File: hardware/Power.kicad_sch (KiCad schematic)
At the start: 39 parts, among them Q1 Q_NMOS, Q2 Q_NMOS, Q3 Q_NMOS, Q4 Q_NMOS, U5 BQ25798RQMR

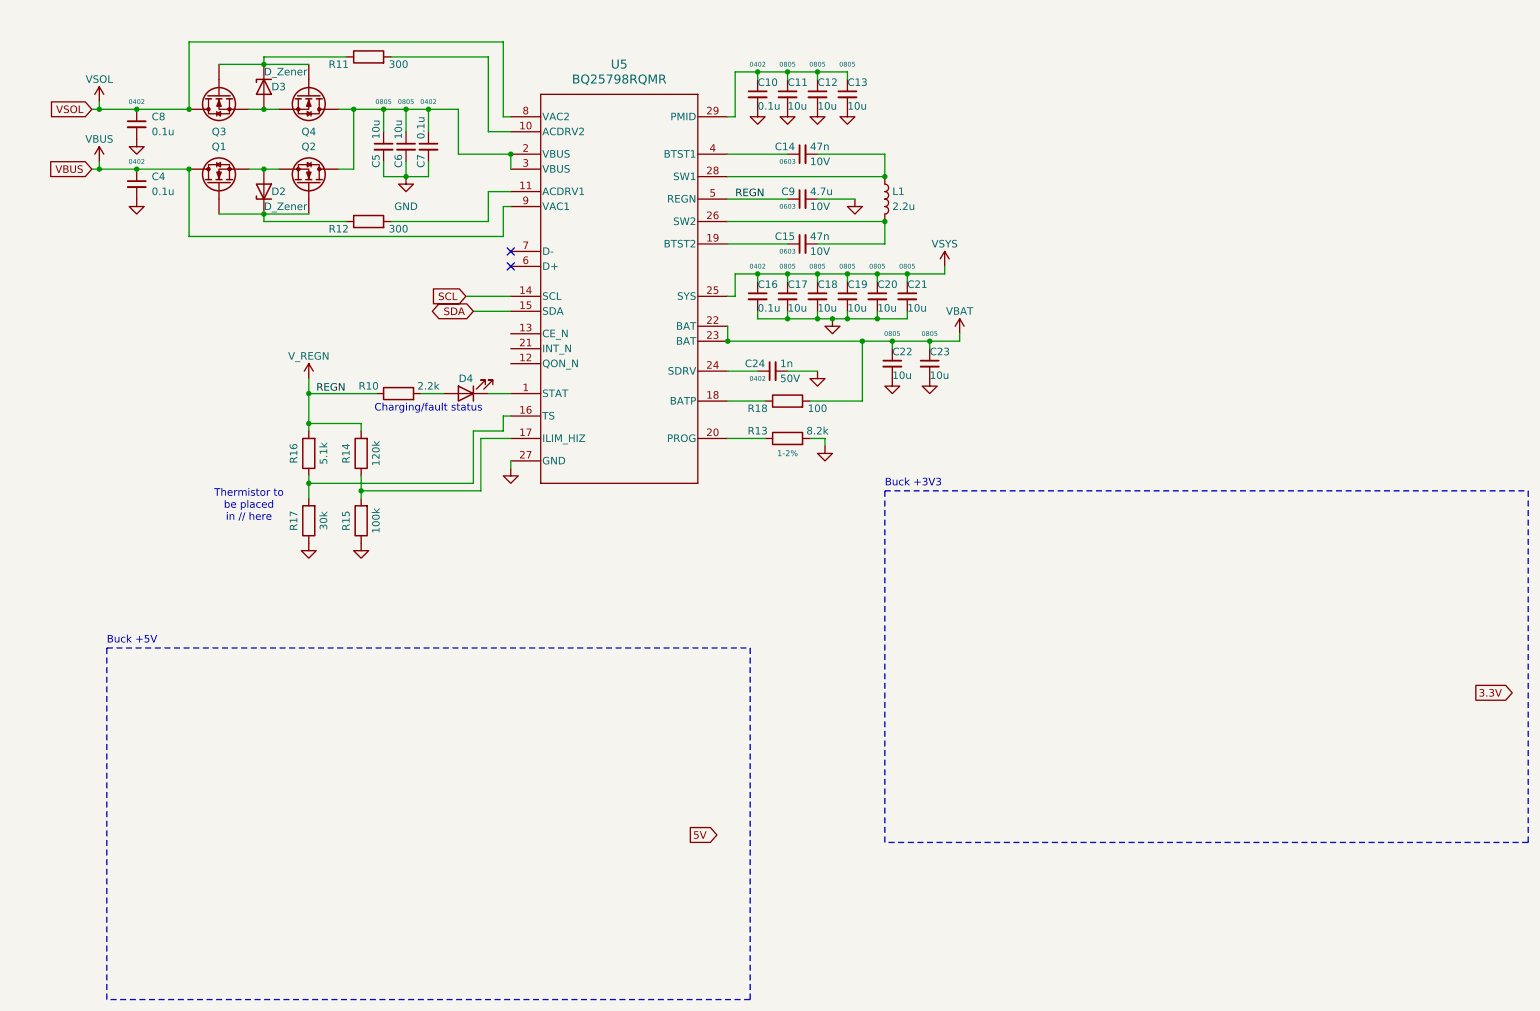
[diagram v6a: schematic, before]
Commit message: Added solar input protection & diodes footprints
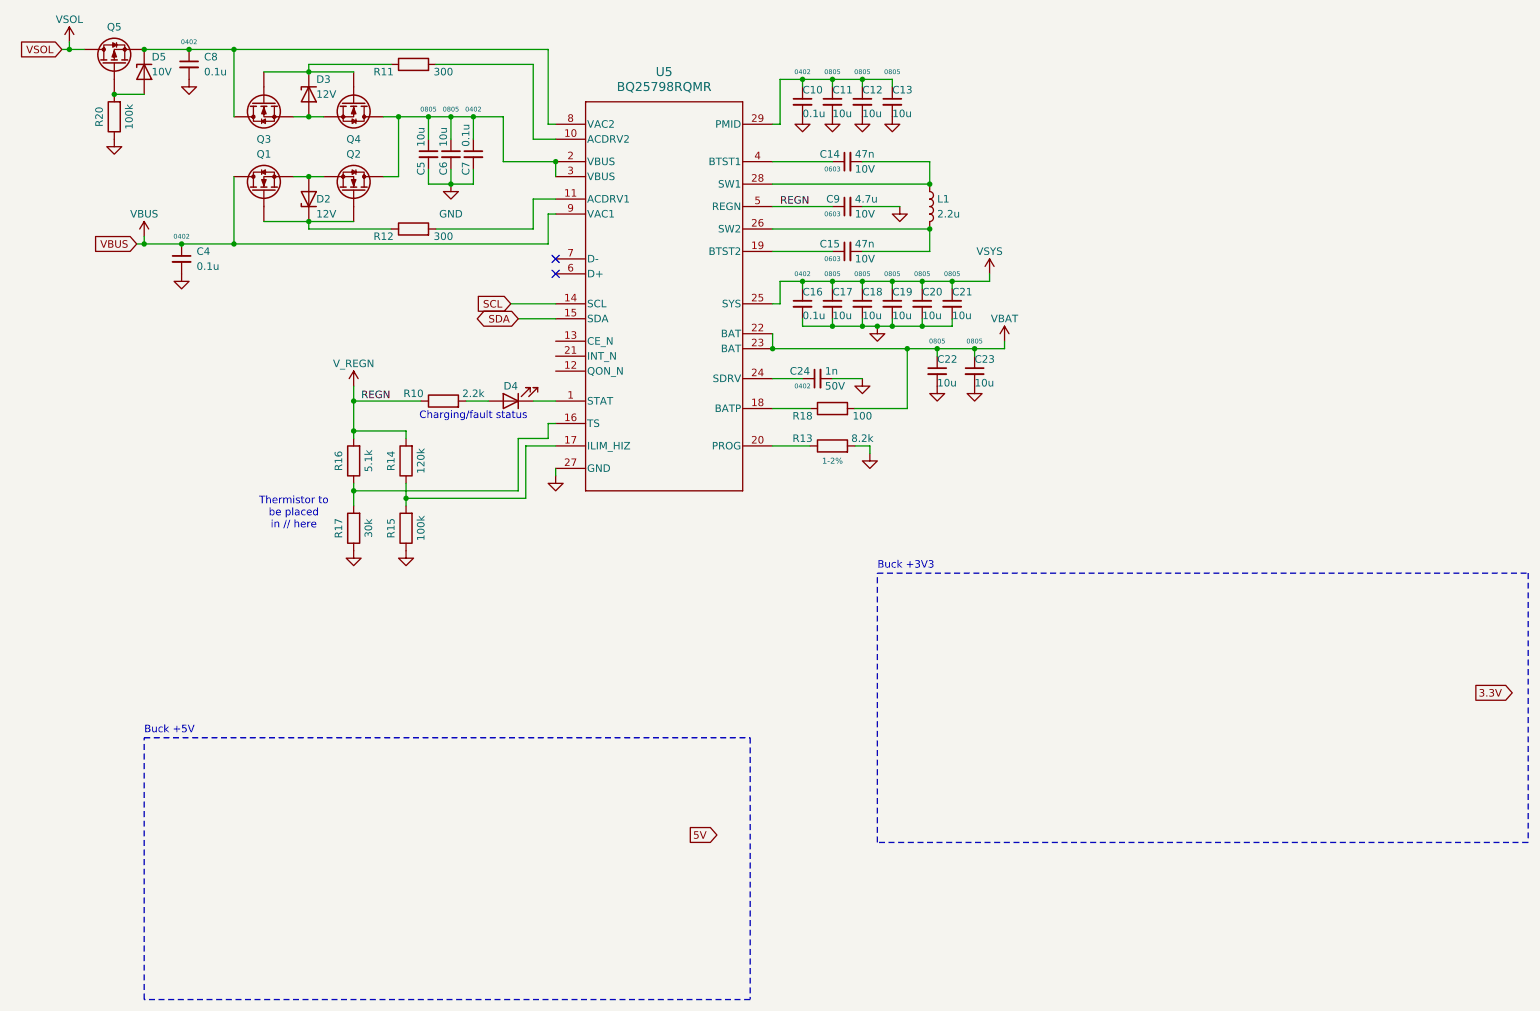
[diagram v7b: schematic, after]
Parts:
- added D5: D_Zener, Diode_SMD:D_SOD-123, symbol Device:D_Zener
- added Q5: Q_PMOS, symbol Device:Q_PMOS
- added R20: 100k, Resistor_SMD:R_0402_1005Metric, symbol Device:R
- D2, D3: footprint (none) -> Diode_SMD:D_SOD-123; Voltage (none) -> 12V
- D4: footprint (none) -> LED_SMD:LED_0603_1608Metric
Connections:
- net GND: now also R20.1
- net VSOL: now also Q5.D; no longer C8.1, Q3.D, U5.8 (VAC2)
- new net: D5.2 (A), Q5.G, R20.2
- new net: C8.1, D5.1 (K), Q3.D, Q5.S, U5.8 (VAC2)
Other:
- moved on the sheet: C10, C11, C12, C13, C14, C15, C16, C17, C18, C19, C20, C21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
